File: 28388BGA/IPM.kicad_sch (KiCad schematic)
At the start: 27 parts, among them CN3 X3025WVS-2*10D-LPSW, Q31 SN74LVC1G125DCKR, Q32 SN74ACT244PWRG4, Q33 FMMT618TA

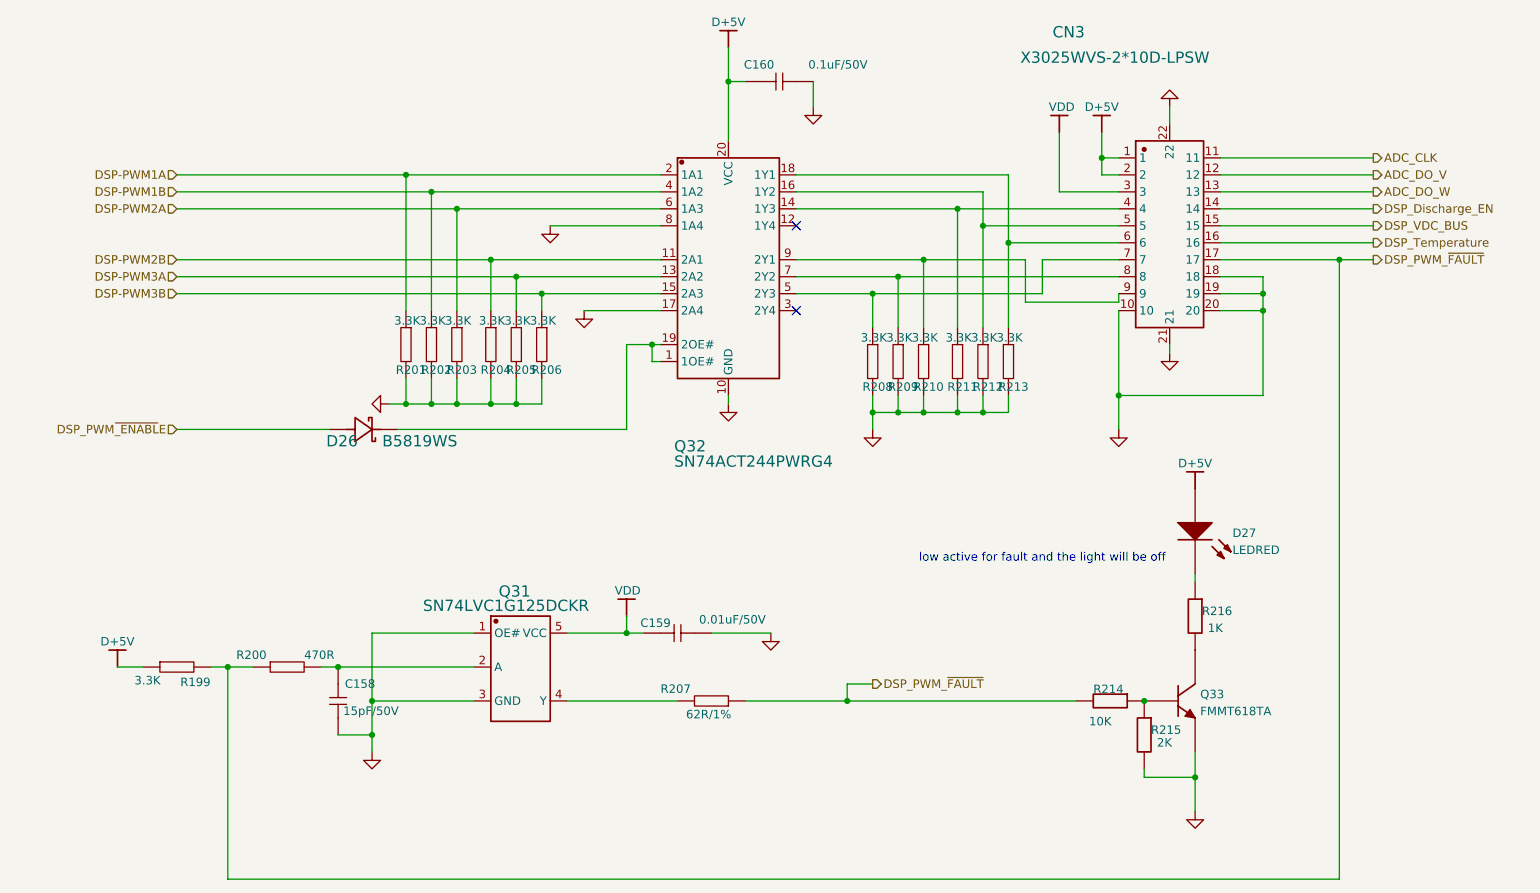
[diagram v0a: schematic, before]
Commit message: 修复AGND BUG
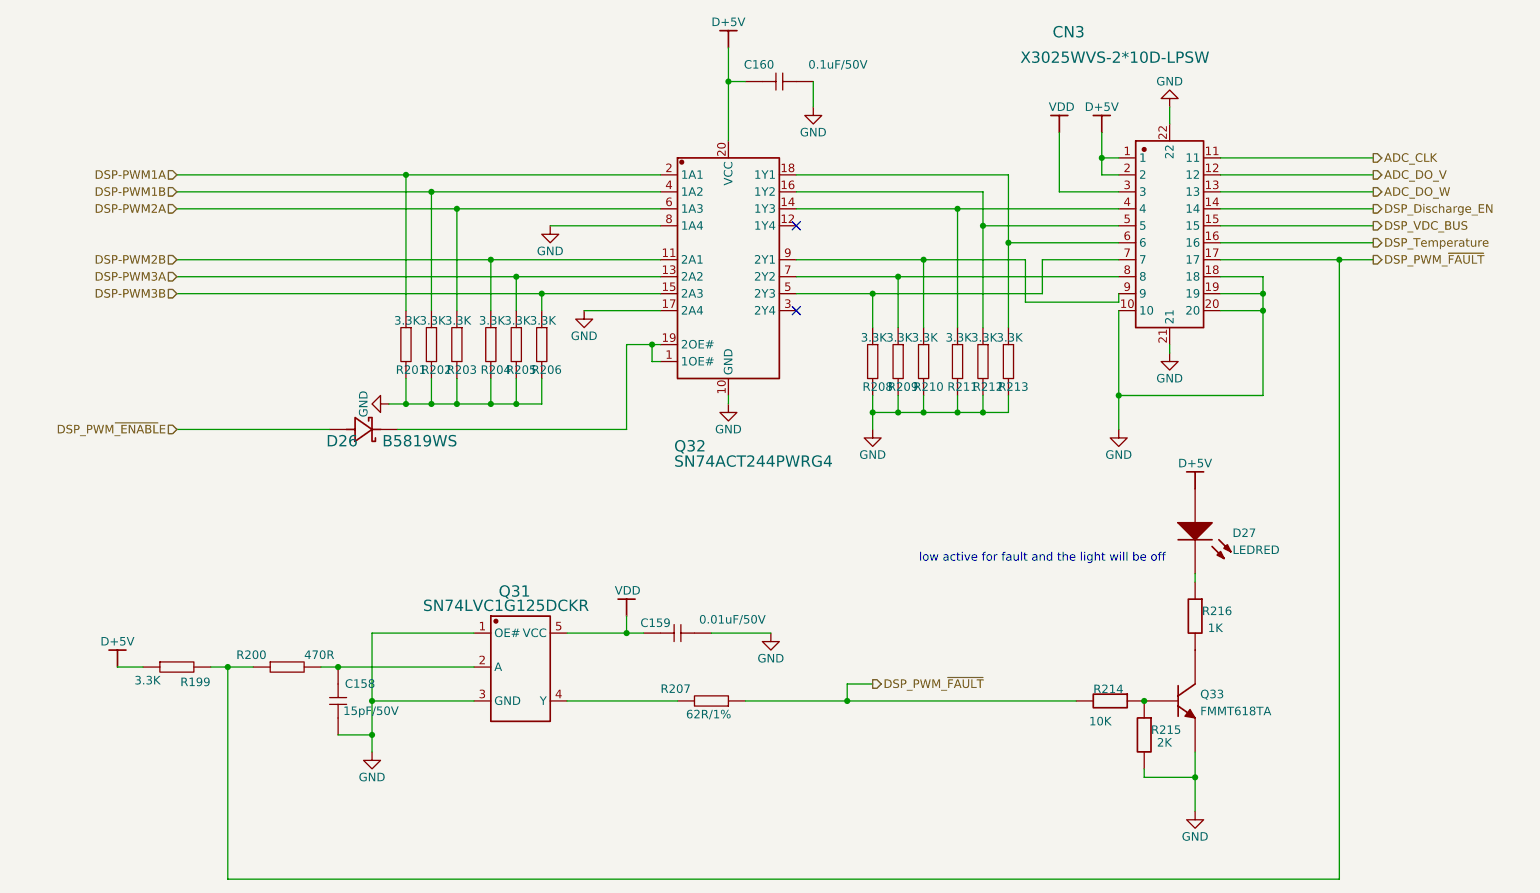
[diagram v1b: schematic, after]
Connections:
- net AGND renamed GND
